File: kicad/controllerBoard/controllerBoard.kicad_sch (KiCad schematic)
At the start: 2 parts, among them J1 Conn_02x20_Top_Bottom, J2 Conn_02x20_Top_Bottom

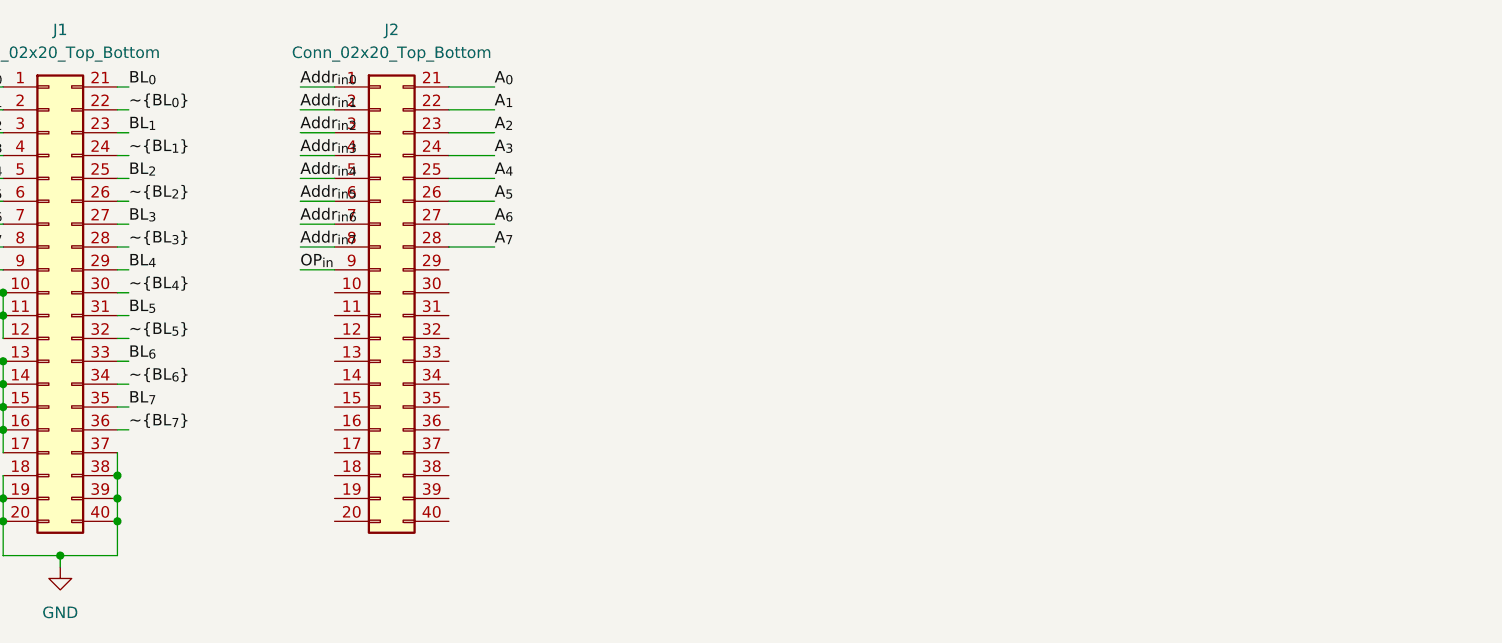
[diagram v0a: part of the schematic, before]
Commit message: finish address to bit line decoder
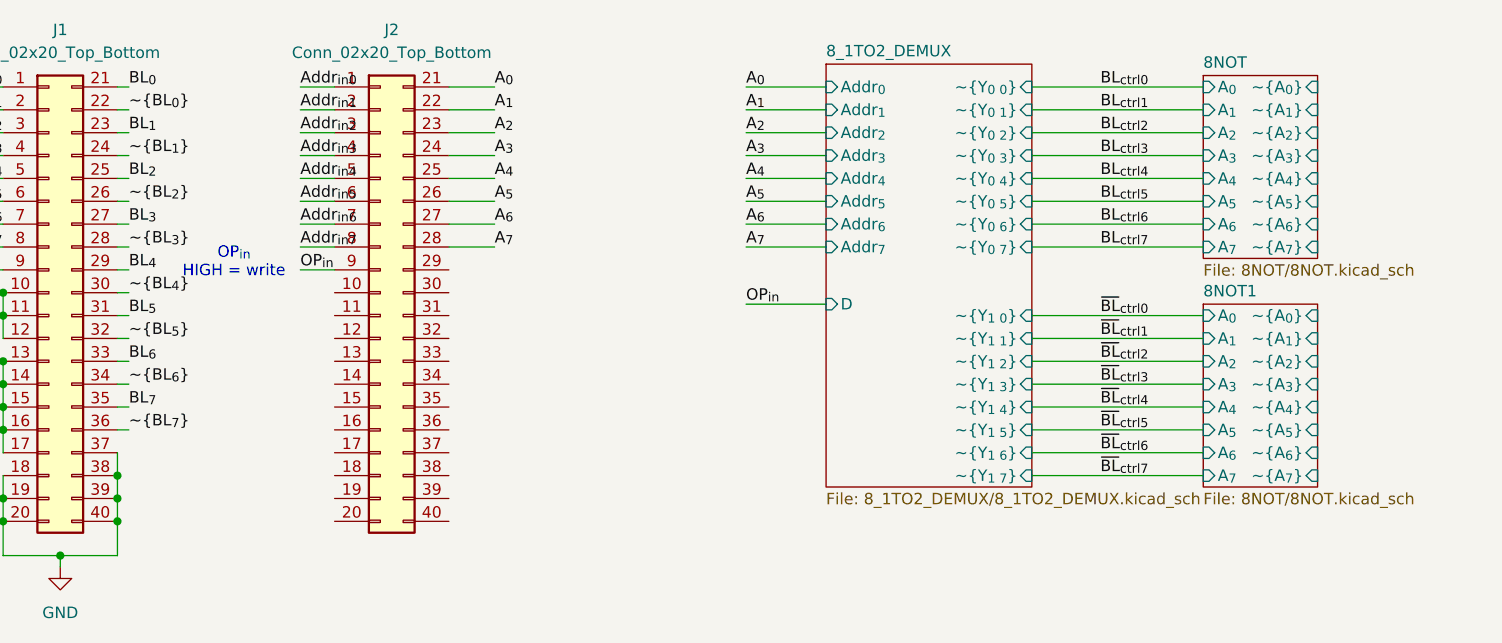
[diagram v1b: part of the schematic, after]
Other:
- added sheet 8NOT (8NOT/8NOT.kicad_sch)
- added sheet 8NOT1 (8NOT/8NOT.kicad_sch)
- added sheet 8_1TO2_DEMUX (8_1TO2_DEMUX/8_1TO2_DEMUX.kicad_sch)
- note added: "OP_{in} HIGH = write"

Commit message: demux
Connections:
- no-connect marks 0 -> 24
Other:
- removed sheet 8NOT
- removed sheet 8NOT1
- added sheet 8DLATCH (8DLATCH\8DLATCH.kicad_sch)
- added sheet 8DLATCH1 (8DLATCH/8DLATCH.kicad_sch)
- added sheet 8DLATCH2 (8DLATCH/8DLATCH.kicad_sch)
- moved on the sheet: J1, J2

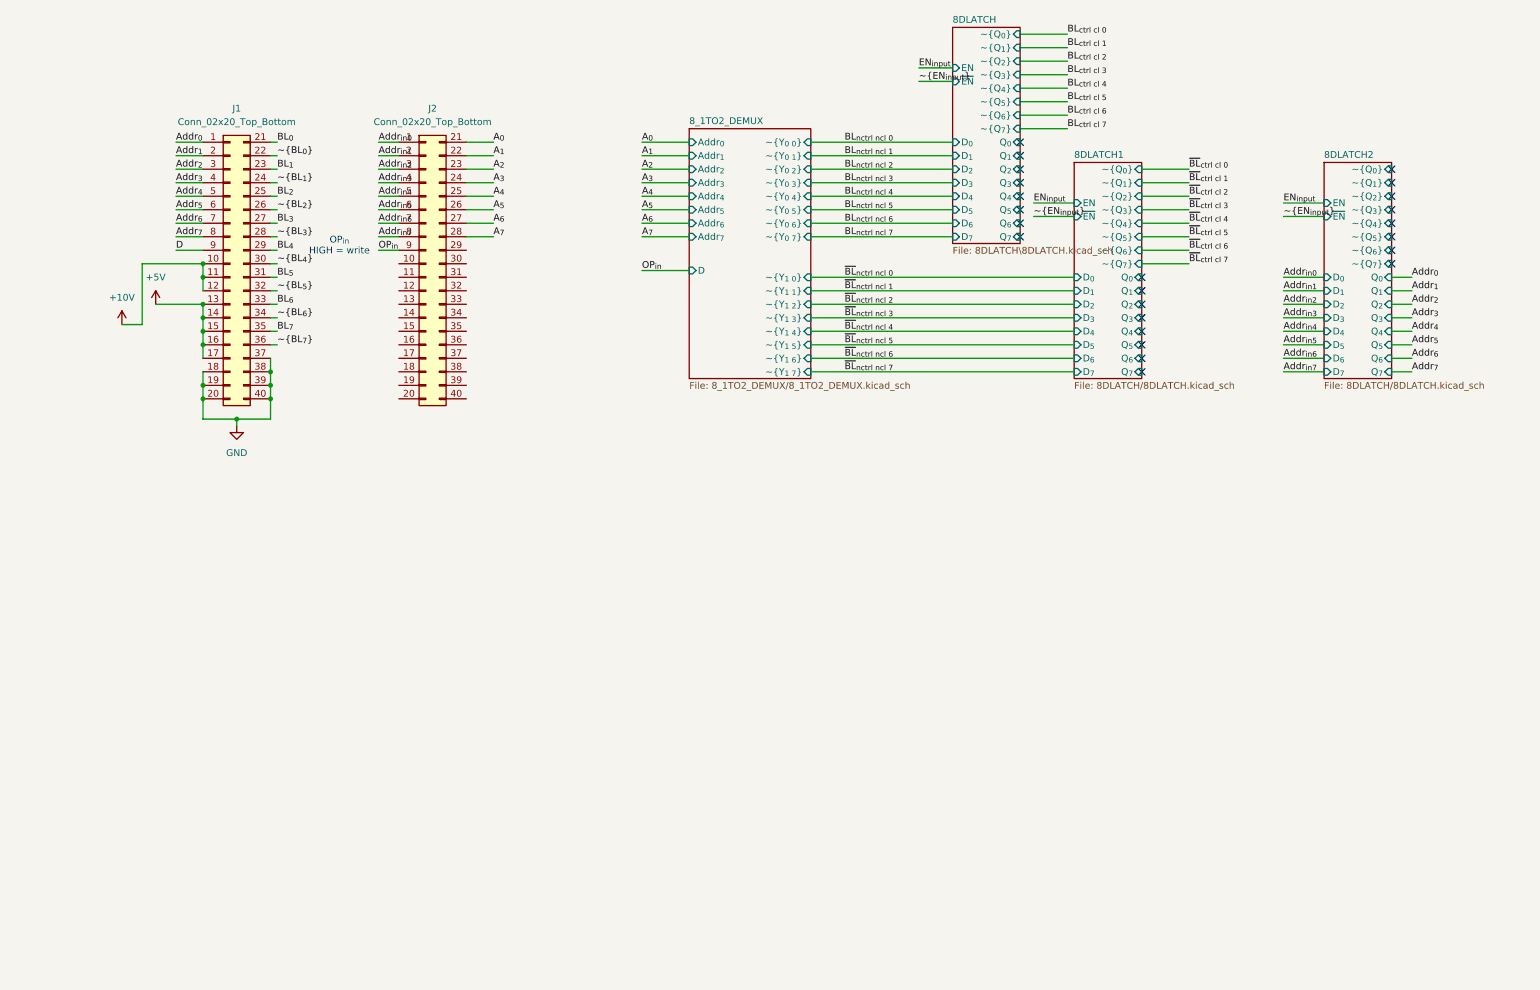
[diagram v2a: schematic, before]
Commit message: Finish input stage schematic
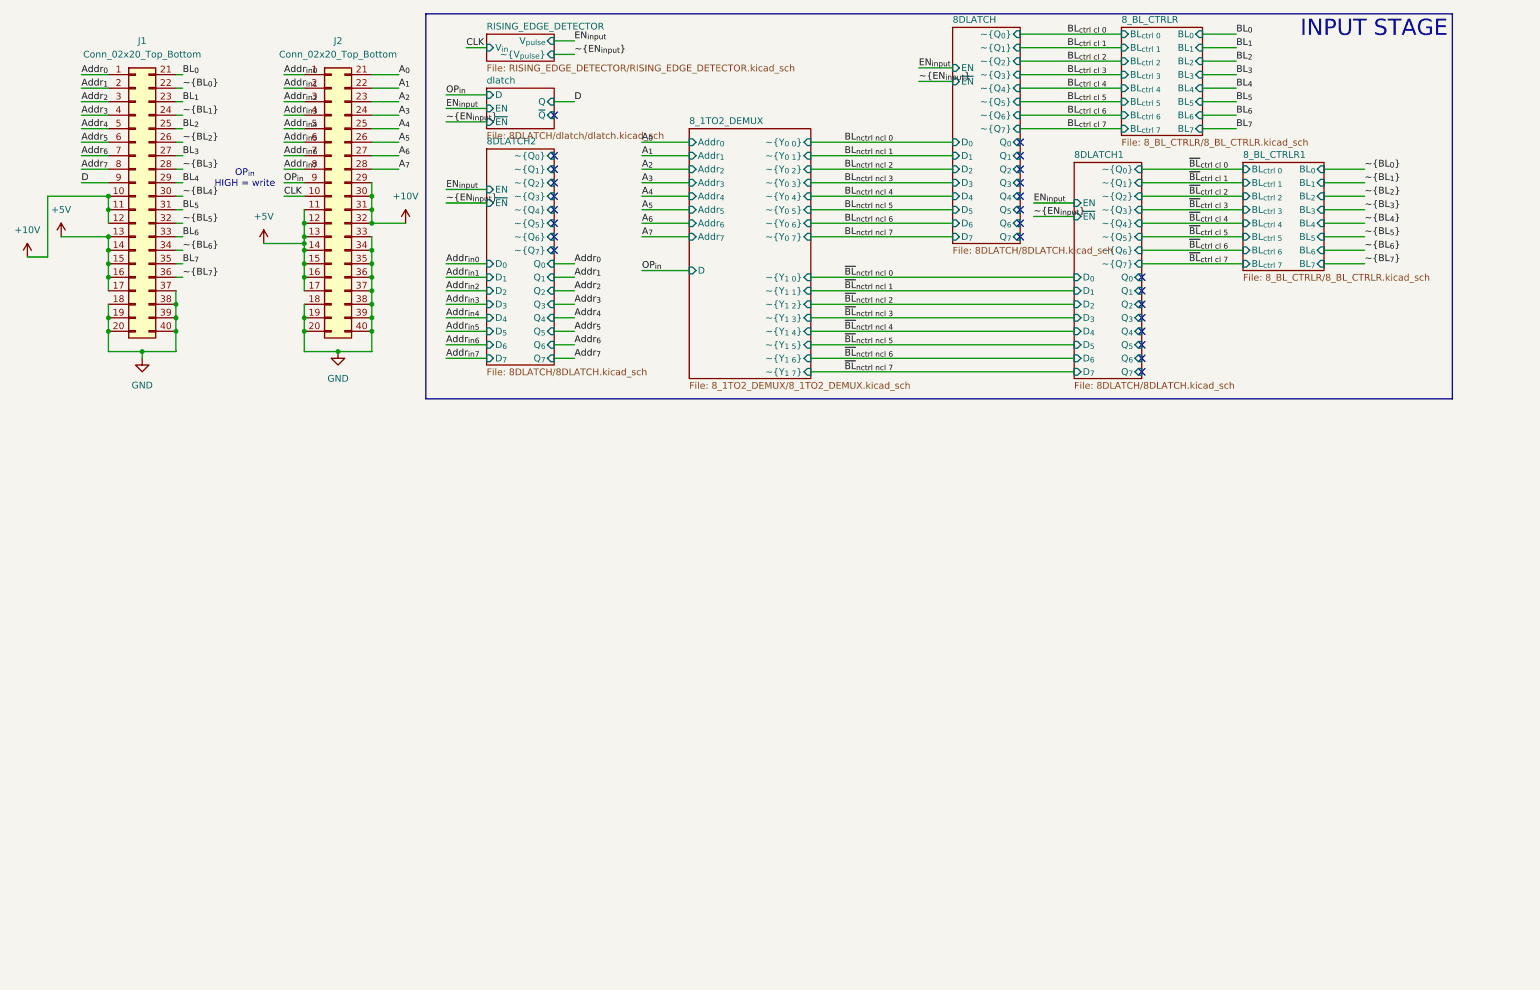
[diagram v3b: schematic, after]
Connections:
- net +10V: now also J2.29 (Pin_29), J2.30 (Pin_30), J2.31 (Pin_31), J2.32 (Pin_32)
- net +5V: now also J2.11 (Pin_11), J2.12 (Pin_12), J2.13 (Pin_13), J2.14 (Pin_14), J2.15 (Pin_15), J2.16 (Pin_16), J2.17 (Pin_17)
- net GND: now also J2.18 (Pin_18), J2.19 (Pin_19), J2.20 (Pin_20), J2.33 (Pin_33), J2.34 (Pin_34), J2.35 (Pin_35), J2.36 (Pin_36), J2.37 (Pin_37), J2.38 (Pin_38), J2.39 (Pin_39), J2.40 (Pin_40)
- net CLK: now reaches J2.10 (Pin_10)
- no-connect marks 24 -> 25
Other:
- added sheet 8_BL_CTRLR (8_BL_CTRLR/8_BL_CTRLR.kicad_sch)
- added sheet 8_BL_CTRLR1 (8_BL_CTRLR/8_BL_CTRLR.kicad_sch)
- added sheet RISING_EDGE_DETECTOR (RISING_EDGE_DETECTOR/RISING_EDGE_DETECTOR.kicad_sch)
- added sheet dlatch (8DLATCH/dlatch/dlatch.kicad_sch)
- sheet 8DLATCH: file 8DLATCH\8DLATCH.kicad_sch -> 8DLATCH/8DLATCH.kicad_sch
- note added: "INPUT STAGE"
- moved on the sheet: J1, J2

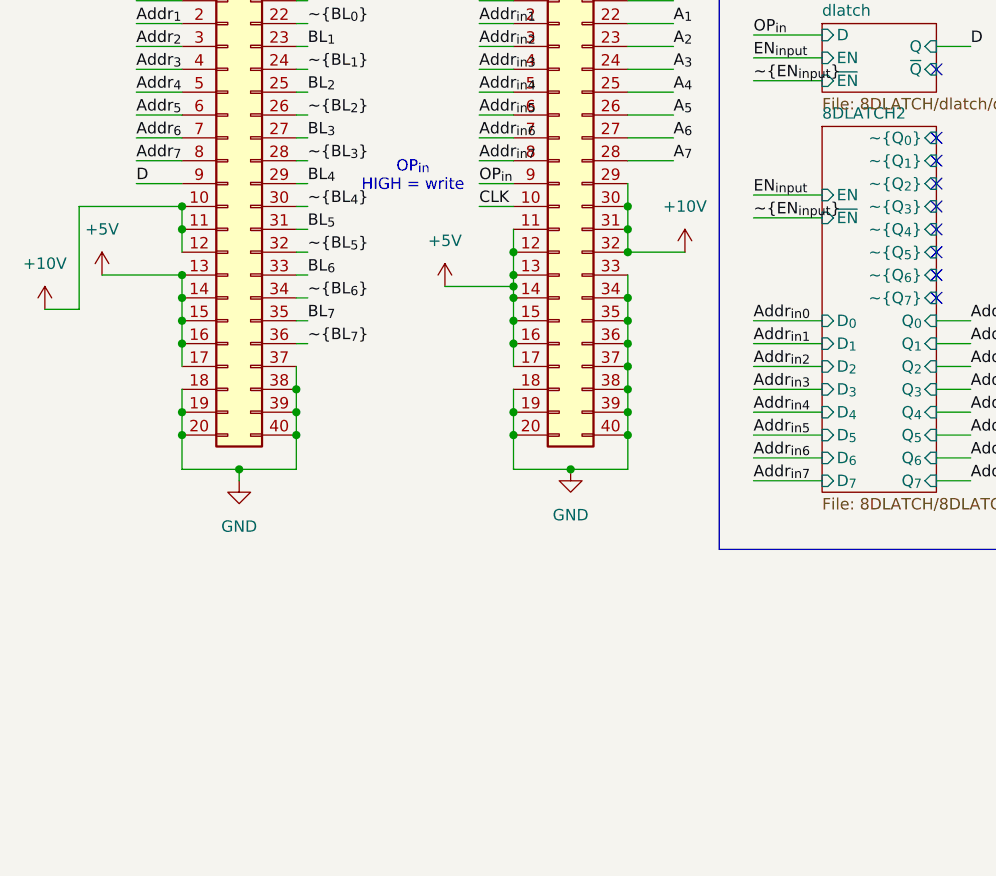
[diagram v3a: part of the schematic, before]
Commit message: simulate rc pulses
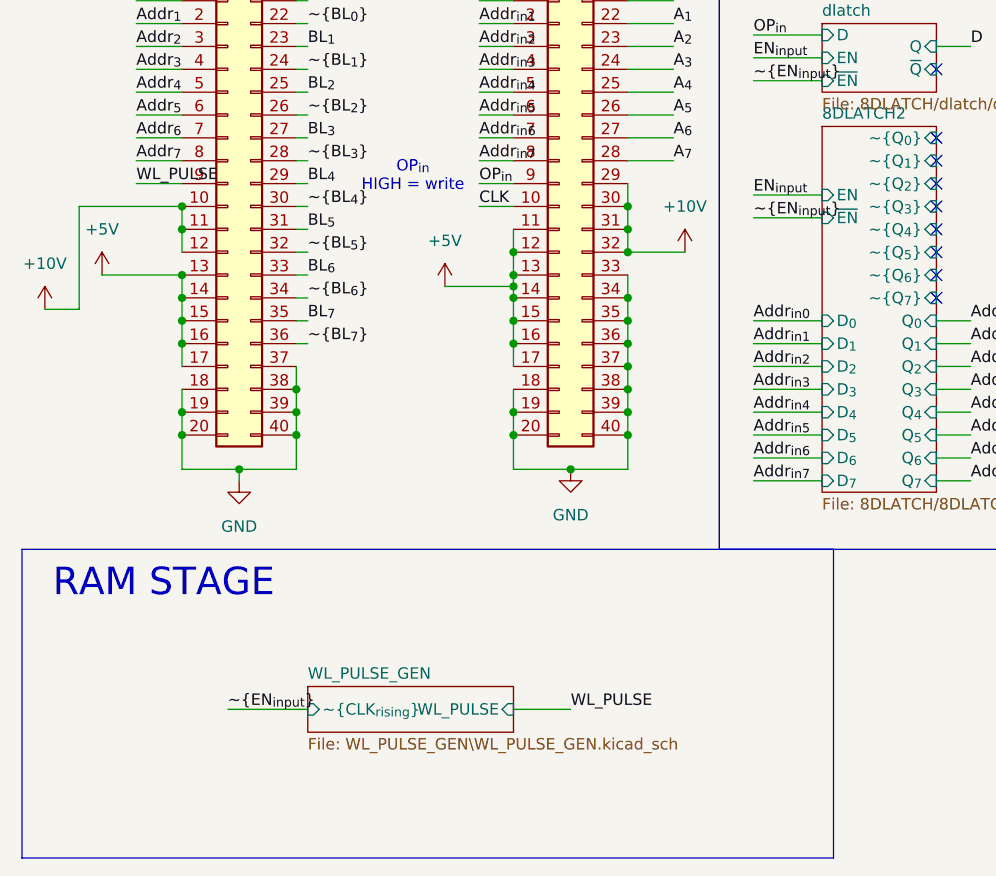
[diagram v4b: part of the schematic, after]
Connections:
- net D: no longer J1.9 (Pin_9)
- new net WL_PULSE: J1.9 (Pin_9)
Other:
- added sheet WL_PULSE_GEN (WL_PULSE_GEN\WL_PULSE_GEN.kicad_sch)
- note added: "RAM STAGE"
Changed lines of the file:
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@@
 	(paper "A4")
 	(rectangle
+		(start 13.97 85.09)
+		(end 104.14 119.38)
+		(stroke
+			(width 0)
+			(type default)
+		)
+		(fill
+			(type none)
+		)
+	)
+	(rectangle
 		(start 91.44 12.7)
 		(end 284.48 85.09)
@@
 		)
 	)
+	(text "RAM STAGE\n"
+		(exclude_from_sim no)
+		(at 29.718 88.9 0)
+		(effects
+			(font
+				(size 3.048 3.048)
+			)
+		)
+	)
 	(junction
 		(at 38.1 76.2)
@@
 	(wire
 		(pts
+			(xy 68.58 102.87) (xy 74.93 102.87)
+		)
+		(stroke
+			(width 0)
+			(type default)
+		)
+	)
+	(wire
+		(pts
 			(xy 81.28 64.77) (xy 81.28 62.23)
 		)
@@
 	(wire
 		(pts
+			(xy 36.83 102.87) (xy 45.72 102.87)
+		)
+		(stroke
+			(width 0)
+			(type default)
+		)
+	)
+	(wire
+		(pts
 			(xy 115.57 77.47) (xy 119.38 77.47)
 		)
@@
 		)
 	)
+	(label "WL_PULSE"
+		(at 74.93 102.87 0)
+		(effects
+			(font
+				(size 1.27 1.27)
+			)
+			(justify left bottom)
+		)
+	)
 	(label "~{BL}_{nctrl ncl 4}"
 		(at 170.18 72.39 0)
@@
 		)
 	)
-	(label "D"
-		(at 26.67 44.45 0)
-		(effects
-			(font
-				(size 1.27 1.27)
-			)
-			(justify left bottom)
-		)
-	)
 	(label "~{BL}_{nctrl ncl 5}"
 		(at 170.18 74.93 0)
@@
 		)
 	)
+	(label "~{EN_{input}}"
+		(at 36.83 102.87 0)
+		(effects
+			(font
+				(size 1.27 1.27)
+			)
+			(justify left bottom)
+		)
+	)
 	(label "Addr_{in}_{1}"
 		(at 64.77 26.67 0)
@@
 		)
 	)
+	(label "WL_PULSE"
+		(at 26.67 44.45 0)
+		(effects
+			(font
+				(size 1.27 1.27)
+			)
+			(justify left bottom)
+		)
+	)
 	(label "Addr_{in}_{4}"
 		(at 95.25 69.85 0)
@@
 				)
 			)
+		)
+	)
+	(sheet
+		(at 45.72 100.33)
+		(size 22.86 5.08)
+		(exclude_from_sim no)
+		(in_bom yes)
+		(on_board yes)
+		(dnp no)
+		(fields_autoplaced yes)
+		(stroke
+			(width 0.1524)
+			(type solid)
+		)
+		(fill
+			(color 0 0 0 0)
+		)
+		(property "Sheetname" "WL_PULSE_GEN"
+			(at 45.72 99.6184 0)
+			(show_name no)
+			(do_not_autoplace no)
+			(effects
+				(font
+					(size 1.27 1.27)
+				)
+				(justify left bottom)
+			)
+		)
+		(property "Sheetfile" "WL_PULSE_GEN\\WL_PULSE_GEN.kicad_sch"
+			(at 45.72 105.9946 0)
+			(show_name no)
+			(do_not_autoplace no)
+			(effects
+				(font
+					(size 1.27 1.27)
+				)
+				(justify left top)
+			)
+		)
+		(pin "WL_PULSE" input
+			(at 68.58 102.87 0)
+			(effects
+				(font
+					(size 1.27 1.27)
+				)
+				(justify right)
+			)
+		)
+		(pin "~{CLK_{rising}}" input
+			(at 45.72 102.87 180)
+			(effects
+				(font
+					(size 1.27 1.27)
+				)
+				(justify left)
+			)
+		)
+		(instances
+			(project "controllerBoard"
+				(path "/93a9a1ca-4ee5-40da-ab67-92836146c003"
+					(page "42")
+				)
+			)

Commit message: finish main schematic
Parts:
- added C10: 330nC, symbol Device:C
- added C11: 15nC, symbol Device:C
- added C12: 180uC, symbol Device:C
- added C13: 100nC, symbol Device:C
- added C14: 470uC, symbol Device:C
- added C9: 10pC, symbol Device:C
- added D5: D, symbol Device:D
- added D6: SMBJ5348B, symbol Device:D_Zener
- added L1: 15uL, symbol Device:L
- added Q635: WTM30N02VD, symbol Simulation_SPICE:NMOS
- added R49: 12mR, symbol Device:R
- added R50: 100R, symbol Device:R
- added R51, R54: 1kR, symbol Device:R
- added R52: 133kR, symbol Device:R
- added R53: 6.98kR, symbol Device:R
- added U1: LM3478MA, Package_SO:SOIC-8_3.9x4.9mm_P1.27mm, symbol Regulator_Controller:LM3478MA
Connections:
- net +10V: now also C12.1, D5.1 (K), D6.1 (K), R53.1; no longer J2.29 (Pin_29), J2.30 (Pin_30), J2.31 (Pin_31), J2.32 (Pin_32)
- net +5V: now also C13.1, C14.1, L1.1, U1.8 (V_{IN}); no longer J2.11 (Pin_11), J2.12 (Pin_12), J2.13 (Pin_13), J2.14 (Pin_14), J2.15 (Pin_15), J2.16 (Pin_16), J2.17 (Pin_17)
- net GND: now also C11.2, C12.2, C13.2, C14.2, C9.2, D6.2 (A), R49.2, R51.2, R52.2, R54.2, U1.4 (AGND), U1.5 (PGND); no longer J2.18 (Pin_18), J2.19 (Pin_19), J2.20 (Pin_20), J2.33 (Pin_33), J2.34 (Pin_34), J2.35 (Pin_35), J2.36 (Pin_36), J2.37 (Pin_37), J2.38 (Pin_38), J2.39 (Pin_39), J2.40 (Pin_40)
- new net: R53.2, R54.1, U1.3 (FB)
- new net: C10.1, C11.1, U1.2 (COMP)
- new net: Q635.3 (S), R49.1, R50.2
- new net: D5.2 (A), L1.2, Q635.1 (D)
- new net: Q635.2 (G), U1.6 (DR)
- new net: C9.1, R50.1, U1.1 (I_{SEN})
- new net: R52.1, U1.7 (FA/SD)
- new net: C10.2, R51.1
- new net Y_{0}: J2.11 (Pin_11)
- new net Y_{1}: J2.12 (Pin_12)
- new net Y_{2}: J2.13 (Pin_13)
- new net Y_{3}: J2.14 (Pin_14)
- new net Y_{4}: J2.15 (Pin_15)
- new net Y_{5}: J2.16 (Pin_16)
- new net Y_{6}: J2.17 (Pin_17)
- new net Y_{7}: J2.18 (Pin_18)
- no-connect marks 25 -> 41
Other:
- added sheet 8DLATCH3 (8DLATCH/8DLATCH.kicad_sch)
- added sheet 8DLATCH4 (8DLATCH/8DLATCH.kicad_sch)
- added sheet READ_LINE_PULSE_GEN (READ_PULSE_GEN/READ_PULSE_GEN.kicad_sch)
- added sheet RISING_EDGE_DETECTOR1 (RISING_EDGE_DETECTOR/RISING_EDGE_DETECTOR.kicad_sch)
- sheet WL_PULSE_GEN: file WL_PULSE_GEN\WL_PULSE_GEN.kicad_sch -> WL_PULSE_GEN/WL_PULSE_GEN.kicad_sch
- note added: "OUTPUT STAGE"
- note added: "POWER MANAGEMENT"
